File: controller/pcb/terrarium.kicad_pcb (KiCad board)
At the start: 4 copper layers, 90 x 90 mm, 78 parts, among them K1 G3MB-202P, K2 G3MB-202P, K3 G3MB-202P, P1 USB_C_Plug_USB2.0, Q1 S8050, Q2 S8050, Q3 S8050, Q4 S8050, Q5 BC817, Q6 BC817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

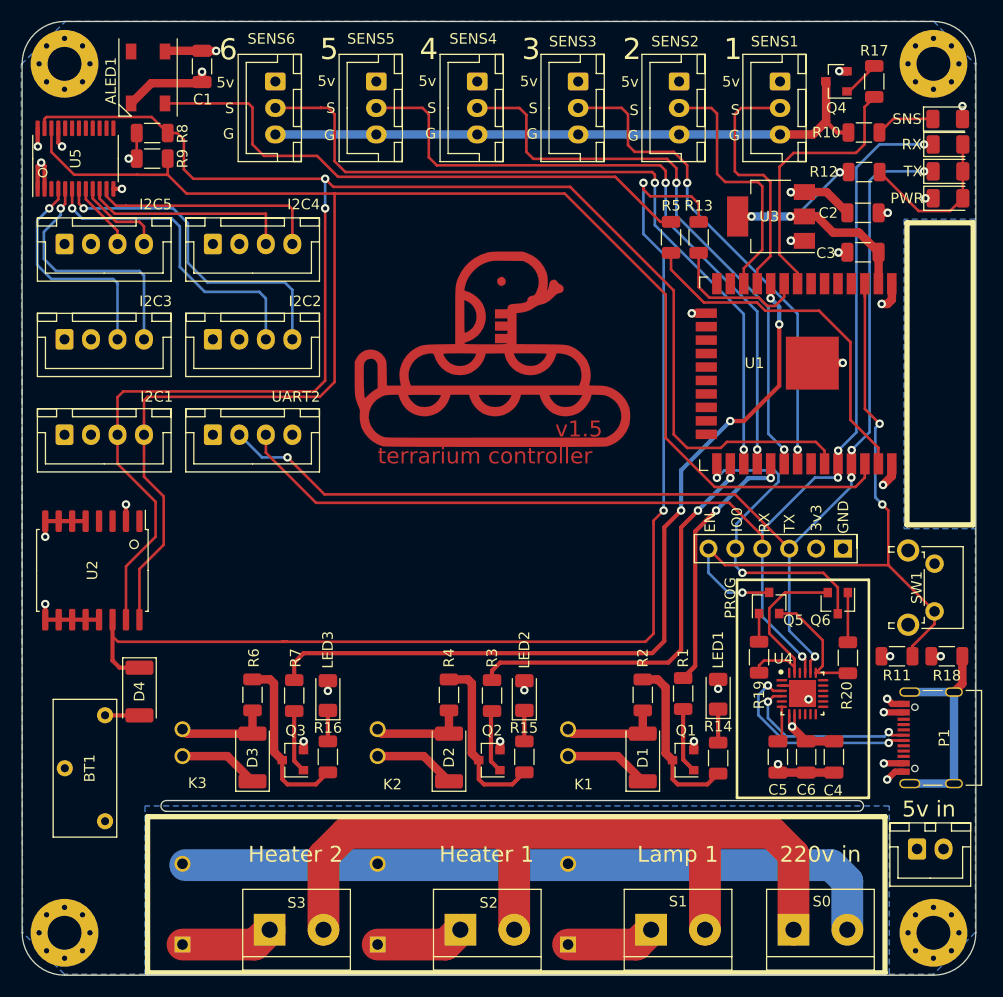
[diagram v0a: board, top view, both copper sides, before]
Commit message: feat: add 5 pin sensor connectors
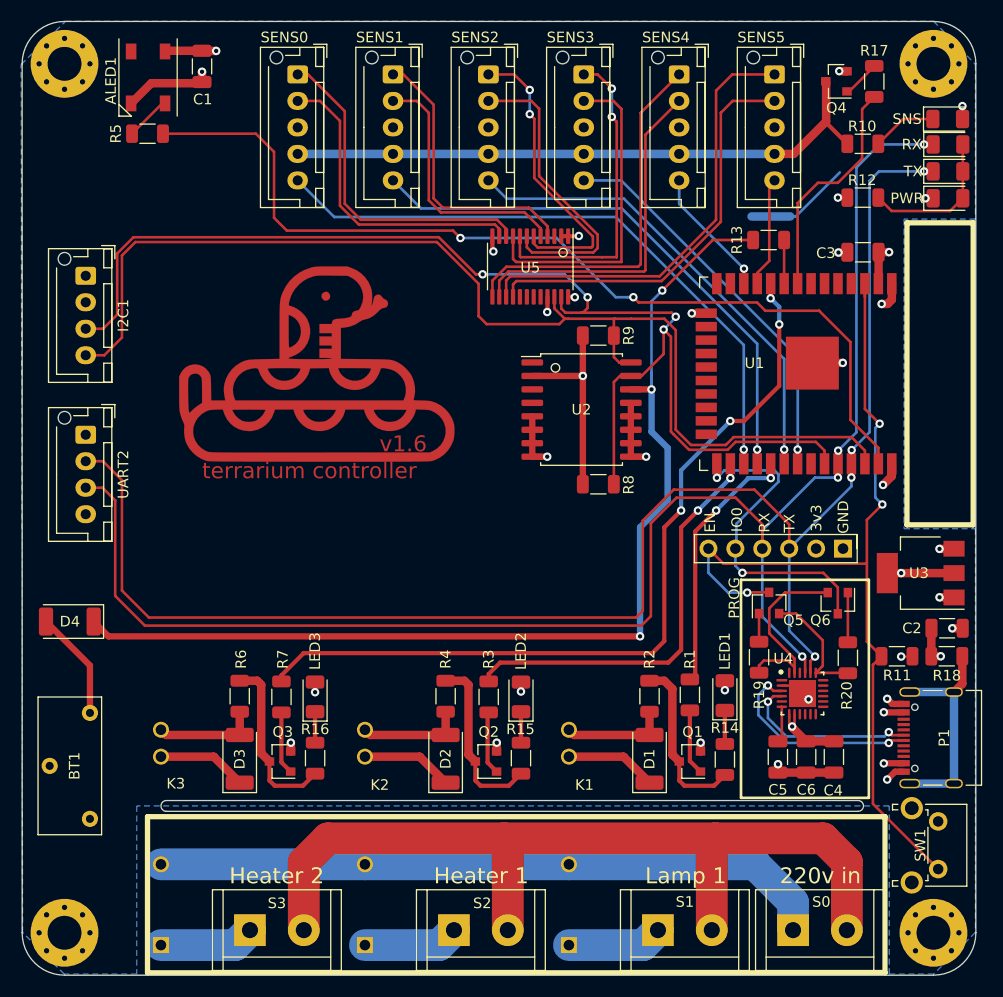
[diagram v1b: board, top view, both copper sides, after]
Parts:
- removed I2C2: 4, Connector_JST:JST_XH_B4B-XH-AM_1x04_P2.50mm_Vertical
- removed I2C3: 3, Connector_JST:JST_XH_B4B-XH-AM_1x04_P2.50mm_Vertical
- removed I2C4: 2, Connector_JST:JST_XH_B4B-XH-AM_1x04_P2.50mm_Vertical
- removed I2C5: 5, Connector_JST:JST_XH_B4B-XH-AM_1x04_P2.50mm_Vertical
- removed S4: PWR, Connector_JST:JST_XH_B2B-XH-AM_1x02_P2.50mm_Vertical
- removed SENS6: 4, Connector_JST:JST_XH_B3B-XH-AM_1x03_P2.50mm_Vertical
- added SENS0: 1, Connector_JST:JST_XH_B5B-XH-AM_1x05_P2.50mm_Vertical, F.Cu at (67.0, 28.0)
- SENS1: value 1 -> 2; footprint Connector_JST:JST_XH_B3B-XH-AM_1x03_P2.50mm_Vertical -> Connector_JST:JST_XH_B5B-XH-AM_1x05_P2.50mm_Vertical
- SENS2: value 2 -> 3; footprint Connector_JST:JST_XH_B3B-XH-AM_1x03_P2.50mm_Vertical -> Connector_JST:JST_XH_B5B-XH-AM_1x05_P2.50mm_Vertical
- SENS3: value 3 -> 4; footprint Connector_JST:JST_XH_B3B-XH-AM_1x03_P2.50mm_Vertical -> Connector_JST:JST_XH_B5B-XH-AM_1x05_P2.50mm_Vertical
- SENS4: value 4 -> 5; footprint Connector_JST:JST_XH_B3B-XH-AM_1x03_P2.50mm_Vertical -> Connector_JST:JST_XH_B5B-XH-AM_1x05_P2.50mm_Vertical
- SENS5: value 4 -> 6; footprint Connector_JST:JST_XH_B3B-XH-AM_1x03_P2.50mm_Vertical -> Connector_JST:JST_XH_B5B-XH-AM_1x05_P2.50mm_Vertical
- moved R8 53.6 mm to (95.4, 66.7)
- moved R5 50.4 mm to (52.8, 33.6), turned to 180 degrees
- moved U2 48.6 mm to (93.8, 59.6), turned to 0 degrees
- moved R9 45.3 mm to (95.4, 52.6)
- moved U5 44.1 mm to (89.0, 46.1), turned to 270 degrees
- moved C2 40.0 mm to (128.3, 80.3), turned to 180 degrees
- moved SENS5 37.6 mm to (112.0, 28.0)
- moved SENS1 36.5 mm to (76.0, 28.0)
- moved U3 36.5 mm to (125.8, 75.1)
- moved SW1 24.3 mm to (127.4, 98.5)
- moved SENS4 19.1 mm to (103.0, 28.0)
- moved SENS2 18.0 mm to (85.0, 28.0)
- moved G*** 16.6 mm to (68.8, 55.3)
- moved I2C1 15.1 mm to (47.0, 47.0), turned to 270 degrees
- moved UART2 12.0 mm to (47.0, 62.0), turned to 270 degrees
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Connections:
- S0 pad 1: 220N -> 220L
- S0 pad 2: 220L -> 220N
- SENS1 pad 1: +5V -> SDA_1
- SENS1 pad 2: G26 -> SCL_1
- SENS1 pad 3: Net-(Q4-Pad3) -> +5V
- SENS2 pad 1: +5V -> SDA_2
- SENS2 pad 2: G27 -> SCL_2
- SENS2 pad 3: Net-(Q4-Pad3) -> +5V
- SENS3 pad 1: +5V -> SDA_3
- SENS3 pad 2: G19 -> SCL_3
- SENS3 pad 3: Net-(Q4-Pad3) -> +5V
- SENS4 pad 1: +5V -> SDA_4
- SENS4 pad 2: G18 -> SCL_4
- SENS4 pad 3: Net-(Q4-Pad3) -> +5V
- SENS5 pad 1: +5V -> SDA_5
- SENS5 pad 2: G17 -> SCL_5
- SENS5 pad 3: Net-(Q4-Pad3) -> +5V
- U5 pad 13: Net-(U5-Pad13) -> SDA_4
- U5 pad 14: Net-(U5-Pad14) -> SCL_4
- U5 pad 15: Net-(U5-Pad15) -> SDA_5
- U5 pad 16: Net-(U5-Pad16) -> SCL_5
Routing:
- net G23: track 33.9 -> 89.2 mm, vias 0 -> 2
- net SCL: track 162.1 -> 108.2 mm
- net Net-(ALED1-Pad4): track 54.7 -> 4.61 mm
- net SDA: track 162.1 -> 117.0 mm, vias 2 -> 4
- net SDA_5: track 0.00 -> 42.1 mm
- net SCL_5: track 0.00 -> 39.1 mm
- net TX: track 113.5 -> 149.4 mm, vias 5 -> 4
- net SDA_4: track 0.00 -> 35.6 mm
- net RX: track 115.4 -> 150.4 mm
- net SCL_4: track 0.00 -> 33.0 mm
- net SDA_3: track 6.43 -> 30.4 mm, vias 0 -> 2
- net SCL_3: track 8.49 -> 30.8 mm
- net EN: track 66.7 -> 86.0 mm
- net G26: track 24.7 -> 11.2 mm
- net G27: track 25.6 -> 13.1 mm, vias 0 -> 1
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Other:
- board text added: "v1.6"
- board text removed: "1"
- board text removed: "2"
- board text removed: "3"
- board text removed: "4"
- board text removed: "5"
- board text removed: "5v in"
- board text removed: "6"
- board text removed: "G"
- board text removed: "S"
- board text removed: "v1.5"

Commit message: wip qnfp28
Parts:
- U4: value CP2102N-A02-GQFN24 -> CP2102N-A02-GQFN28; footprint cp2102:Silicon_Labs-CP2102N-A02-GQFN24-IPC_A -> cp2102:Silicon_Labs-CP2102N-A02-GQFN28-IPC_A
- moved R20 0.76 mm to (119.1, 82.3)
- moved R19 0.70 mm to (110.5, 82.3)
- moved U4 0.49 mm to (115.1, 86.7)
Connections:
- U4 pad 19: Net-(Q5-Pad2) -> Net-(U4-Pad19)
- U4 pad 2: GND -> Net-(U4-Pad2)
- U4 pad 20: TX -> Net-(U4-Pad20)
- U4 pad 21: RX -> Net-(U4-Pad21)
- U4 pad 23: Net-(Q6-Pad2) -> Net-(U4-Pad23)
- U4 pad 24: Net-(U4-Pad24) -> Net-(Q5-Pad2)
- U4 pad 25: GND -> TX
- U4 pad 3: Net-(P1-PadA6) -> GND
- U4 pad 4: Net-(P1-PadA7) -> Net-(P1-PadA6)
- U4 pad 5: Net-(U4-Pad5) -> Net-(P1-PadA7)
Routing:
- net Net-(Q5-Pad2): track 11.6 -> 5.15 mm
- net Net-(Q6-Pad2): track 18.2 -> 15.6 mm
- net TX: track 149.4 -> 147.6 mm
- net RX: track 150.4 -> 148.8 mm
- net Net-(C5-Pad1): track 3.41 -> 4.78 mm
- net SDA_3: track 30.4 -> 31.6 mm
- net SCL_3: track 30.8 -> 31.6 mm
- net Net-(Q5-Pad1): track 2.66 -> 1.96 mm
- net Net-(Q6-Pad1): track 4.69 -> 4.00 mm
- net +5V: track 48.6 -> 48.0 mm
- added copper zone on In1.Cu, net +5V
- removed copper zone on In1.Cu, net GND

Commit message: rearrange components
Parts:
- added PWR1: data, Connector_PinHeader_2.54mm:PinHeader_1x01_P2.54mm_Vertical, F.Cu at (118.5, 70.1)
- I2C1: value 1 -> LCD
- moved C3 1.27 mm to (120.3, 43.5)
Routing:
- net Net-(Q5-Pad2): track 5.15 -> 13.1 mm
- net GND: track 58.3 -> 60.9 mm
- net RX: track 148.8 -> 150.1 mm
- net +3V3: track 42.0 -> 43.3 mm
- net +5V: track 48.0 -> 49.3 mm
- net TX: track 147.6 -> 148.9 mm
- added copper zone on In2.Cu, net GND
- removed copper zone on In2.Cu, net +5V

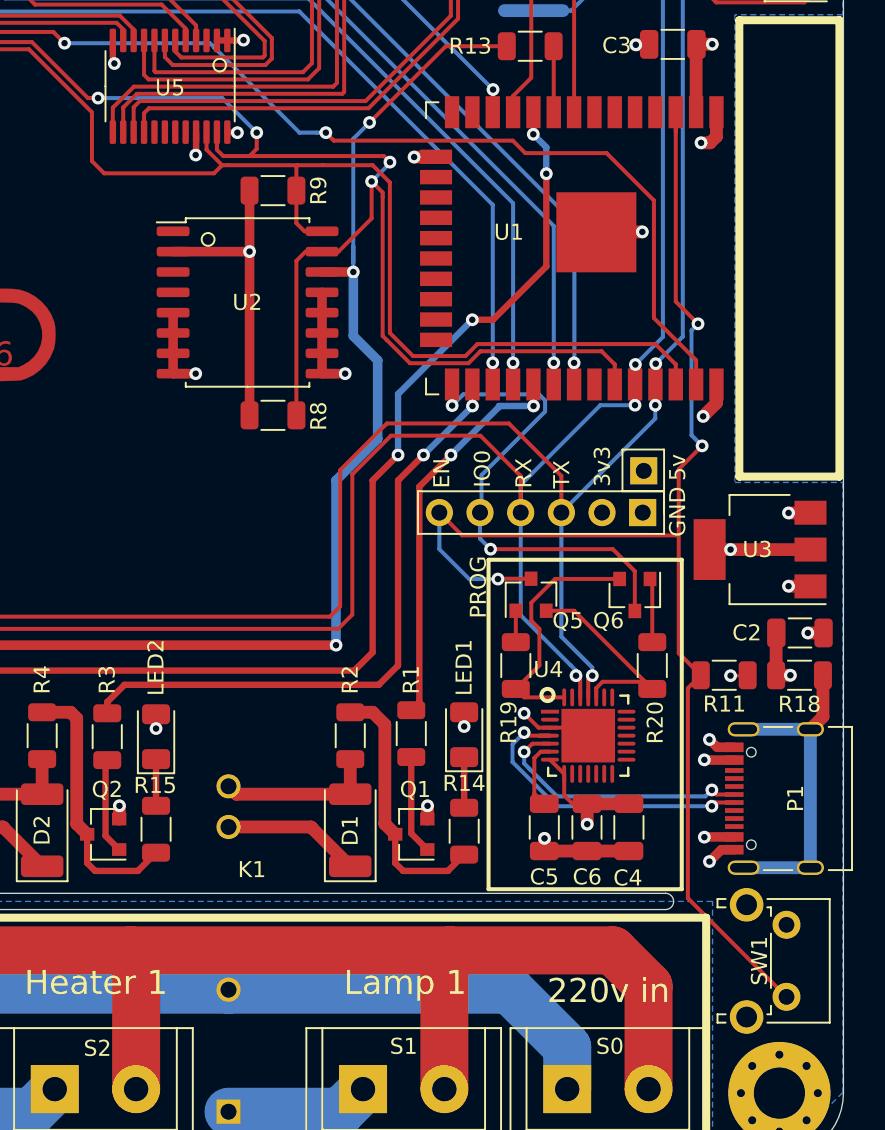
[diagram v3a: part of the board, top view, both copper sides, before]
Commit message: fix bugs, update button footprint
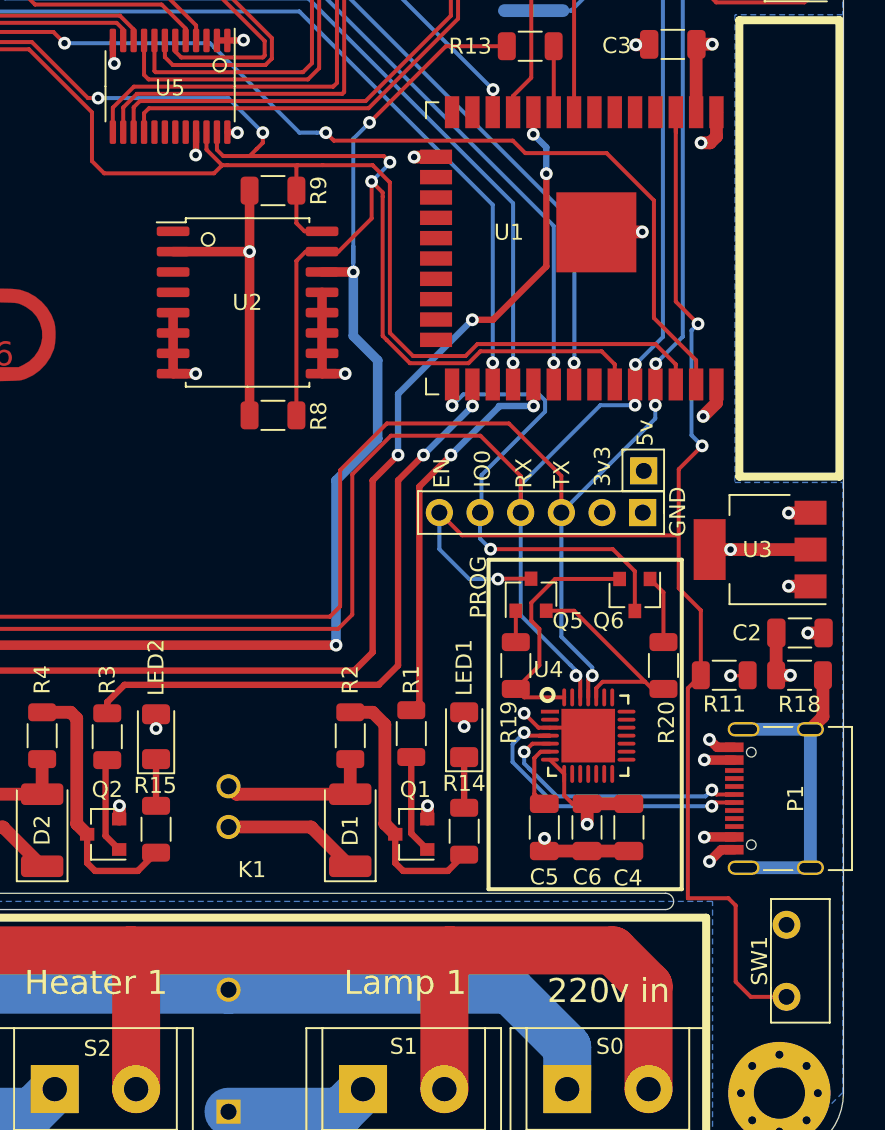
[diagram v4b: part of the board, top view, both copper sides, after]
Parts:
- moved R20 0.70 mm to (119.8, 82.3)
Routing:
- net EN: track 86.0 -> 88.8 mm
- net Net-(Q5-Pad2): track 13.1 -> 12.4 mm
- net SDA: track 117.0 -> 117.6 mm

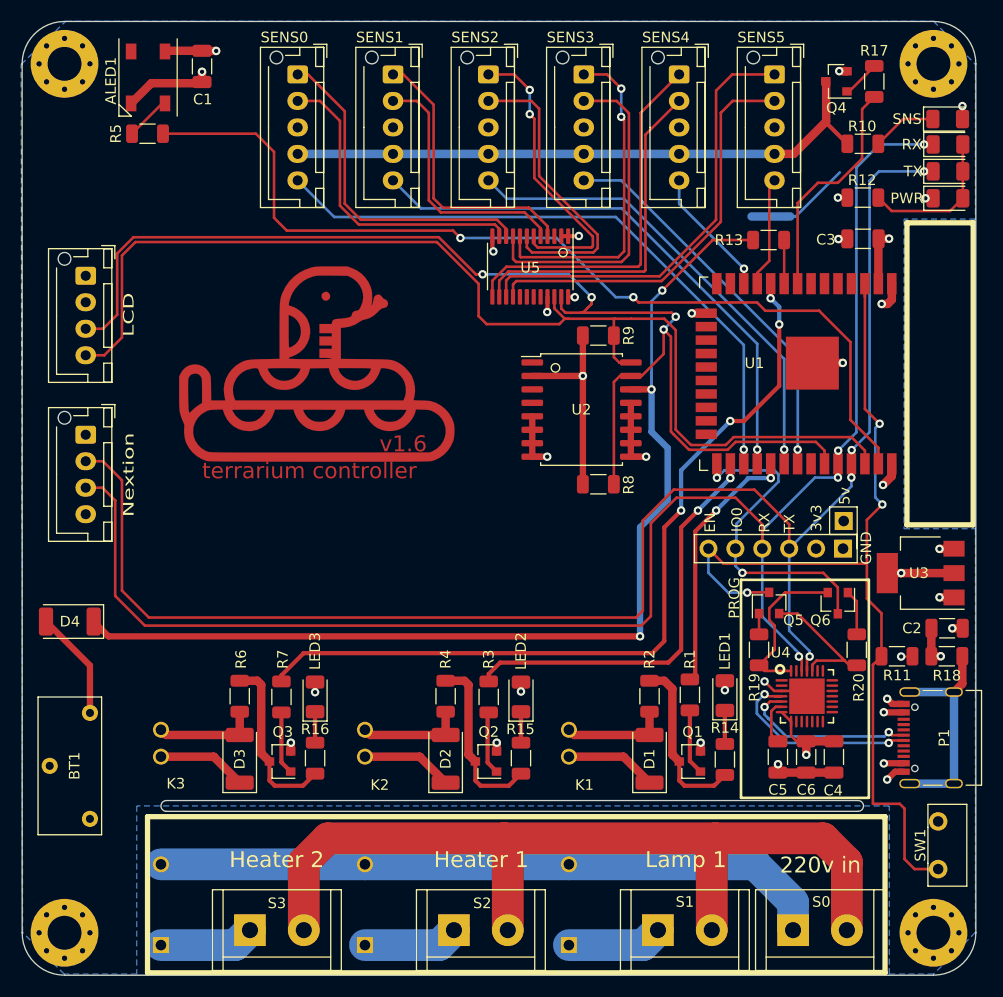
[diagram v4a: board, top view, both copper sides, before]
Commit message: update ssr circuits
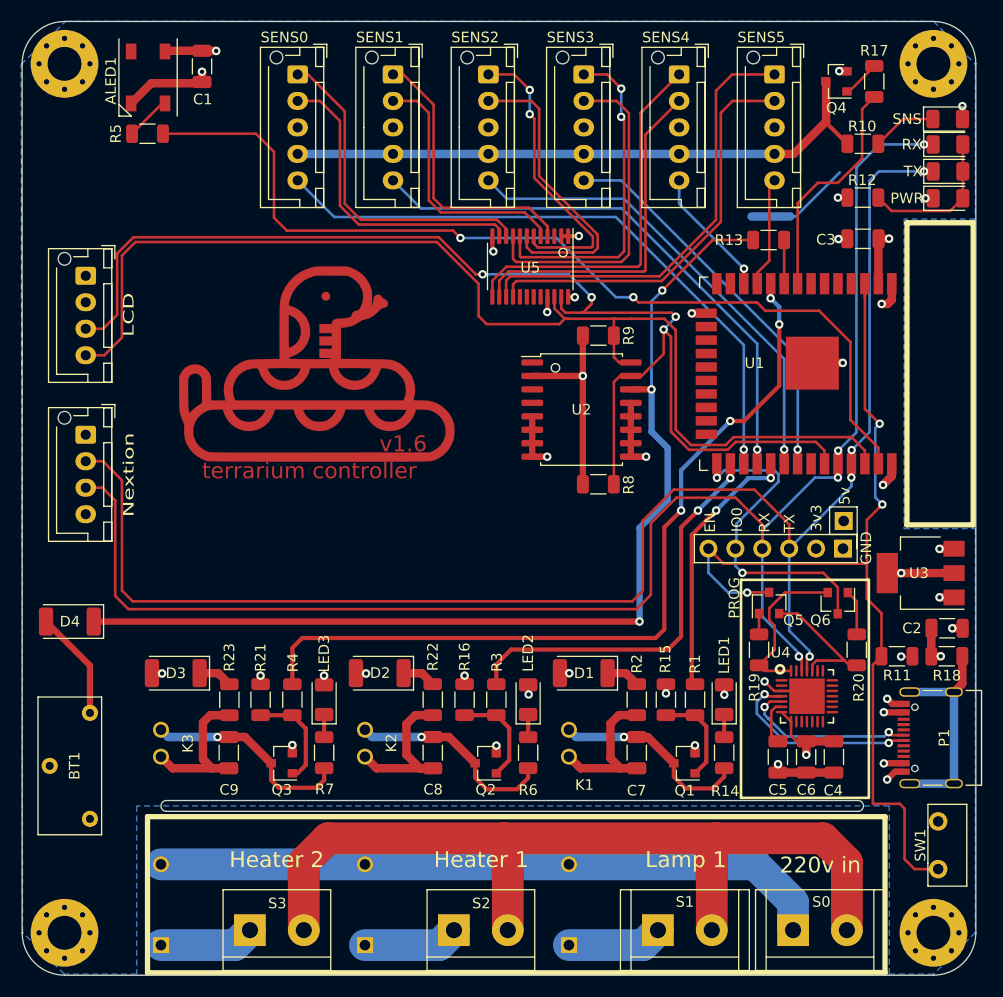
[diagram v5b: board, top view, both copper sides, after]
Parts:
- added C7: 10nF, Capacitor_SMD:C_1206_3216Metric, F.Cu at (99.0, 92.0)
- added C8: 10nF, Capacitor_SMD:C_1206_3216Metric, F.Cu at (79.8, 92.0)
- added C9: 10nF, Capacitor_SMD:C_1206_3216Metric, F.Cu at (60.5, 92.0)
- added R21: 10k, Resistor_SMD:R_1206_3216Metric, F.Cu at (63.5, 87.0)
- added R22: 10, Resistor_SMD:R_1206_3216Metric, F.Cu at (79.8, 87.0)
- added R23: 10, Resistor_SMD:R_1206_3216Metric, F.Cu at (60.6, 87.0)
- K2, K3: footprint Omron:RELAY_G3MB-202P -> omron:RELAY_G3MB-202P
- R15, R16: value 5k -> 10k
- R4: value 10 -> 150ohm
- R6: value 10 -> 5k
- R7: value 150ohm -> 5k
- S2: value Heater 1 Out -> Lamp 1 Out
- S3: value Heater 2 Out -> Lamp 1 Out
- moved R6 27.7 mm to (88.8, 92.0)
- moved R16 15.1 mm to (82.8, 87.0)
- moved R15 14.7 mm to (101.8, 87.0)
- moved R4 14.5 mm to (66.5, 87.0)
- moved D2 10.2 mm to (74.8, 84.5), turned to 180 degrees
- moved D1 10.2 mm to (94.0, 84.5), turned to 180 degrees
- moved D3 10.1 mm to (55.5, 84.5), turned to 180 degrees
- moved R7 6.63 mm to (69.5, 92.0)
- moved R2 1.24 mm to (99.0, 87.0)
- moved LED3 0.90 mm to (69.5, 87.0)
- moved R3 0.77 mm to (85.8, 87.0)
- moved LED2 0.72 mm to (88.8, 87.0)
- moved R1 0.66 mm to (104.5, 87.0)
- moved R14 0.65 mm to (107.2, 92.0)
- moved Q1 0.54 mm to (103.5, 93.0)
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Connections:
- D1 pad 1: +5V -> Net-(D1-Pad1)
- D1 pad 2: Net-(D1-Pad2) -> +5V
- D2 pad 1: +5V -> Net-(D2-Pad1)
- D2 pad 2: Net-(D2-Pad2) -> +5V
- D3 pad 1: +5V -> Net-(D3-Pad1)
- D3 pad 2: Net-(D3-Pad2) -> +5V
- K1 pad 3: +5V -> Net-(C7-Pad1)
- K1 pad 4: Net-(D1-Pad2) -> Net-(C7-Pad2)
- K2 pad 3: +5V -> Net-(C8-Pad1)
- K2 pad 4: Net-(D2-Pad2) -> Net-(C8-Pad2)
- K3 pad 3: +5V -> Net-(C9-Pad1)
- K3 pad 4: Net-(D3-Pad2) -> Net-(C9-Pad2)
- Q1 pad 3: Net-(Q1-Pad3) -> Net-(C7-Pad2)
- Q2 pad 3: Net-(Q2-Pad3) -> Net-(C8-Pad2)
- Q3 pad 3: Net-(Q3-Pad3) -> Net-(C9-Pad2)
- R14 pad 2: Net-(Q1-Pad3) -> Net-(C7-Pad2)
- R15 pad 1: Net-(LED2-Pad1) -> GND
- R15 pad 2: Net-(Q2-Pad3) -> Net-(Q1-Pad1)
- R16 pad 1: Net-(LED3-Pad1) -> GND
- R16 pad 2: Net-(Q3-Pad3) -> Net-(Q2-Pad1)
- R2 pad 1: Net-(Q1-Pad3) -> Net-(D1-Pad1)
- R2 pad 2: Net-(D1-Pad2) -> Net-(C7-Pad1)
- R4 pad 1: Net-(Q2-Pad3) -> G25
- R4 pad 2: Net-(D2-Pad2) -> Net-(Q3-Pad1)
- R6 pad 1: Net-(Q3-Pad3) -> Net-(LED2-Pad1)
- R6 pad 2: Net-(D3-Pad2) -> Net-(C8-Pad2)
- R7 pad 1: G25 -> Net-(LED3-Pad1)
- R7 pad 2: Net-(Q3-Pad1) -> Net-(C9-Pad2)
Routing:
- net +5V: track 49.3 -> 26.0 mm, vias 10 -> 13
- net Net-(C9-Pad2): track 0.00 -> 20.0 mm, vias 0 -> 1
- net Net-(C8-Pad2): track 0.00 -> 19.9 mm, vias 0 -> 1
- net Net-(C7-Pad2): track 0.00 -> 19.0 mm, vias 0 -> 1
- net Net-(Q2-Pad3): track 16.6 -> 0.00 mm
- net Net-(Q3-Pad3): track 16.5 -> 0.00 mm
- net Net-(Q1-Pad3): track 16.3 -> 0.00 mm
- net Net-(C8-Pad1): track 0.00 -> 15.6 mm
- net Net-(C9-Pad1): track 0.00 -> 14.3 mm
- net Net-(C7-Pad1): track 0.00 -> 14.3 mm
- net Net-(D2-Pad2): track 10.0 -> 0.00 mm
- net Net-(D1-Pad2): track 10.00 -> 0.00 mm
- net Net-(D3-Pad2): track 9.83 -> 0.00 mm
- net Net-(Q3-Pad1): track 5.95 -> 9.82 mm
- net Net-(Q2-Pad1): track 5.98 -> 9.50 mm
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
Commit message: release
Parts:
- added ?: , , F.Cu at (61.7, 28.1)
- moved G*** 3.58 mm to (69.2, 58.9)
- moved C3 0.06 mm to (120.3, 43.6)
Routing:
- net 220N: track 83.6 -> 86.0 mm
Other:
- outline, holes or cut-outs redrawn
- board text added: "5V"
- board text added: "SIG"
- board text added: "terrarium controller v1.6 github.com/brushknight/terrarium github.com/brushknight/terrarium-hardware"
- board text removed: "terrarium controller v1.5 github.com/brushknight/terrarium github.com/brushknight/terrarium-hardware"
